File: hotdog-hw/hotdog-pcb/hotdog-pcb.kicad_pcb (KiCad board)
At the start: 2 copper layers, 202.5 x 50 mm, 29 parts, among them J1 Conn_01x01, J2 Conn_01x01, J3 Conn_01x01, J4 Conn_01x01, SW1 SW_SPST, U1 NRF24L01_Breakout, U2 ME2108A

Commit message: Simplify PCB
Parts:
- SW1: footprint Button_Switch_THT:SW_Tactile_SPST_Angled_PTS645Vx58-2LFS -> Button_Switch_THT:SW_CuK_OS102011MA1QN1_SPDT_Angled
- moved SW1 5.99 mm to (247.5, 60.0), turned to 90 degrees
- moved R6 3.54 mm to (72.5, 67.5)
- moved J1 2.50 mm to (55.0, 67.5)
- moved J2 2.50 mm to (55.0, 72.5)
- moved J3 2.50 mm to (247.5, 72.5)
- moved J4 2.50 mm to (247.5, 67.5)
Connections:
- J3 pad 1: Net-(A1-Pad4) -> Net-(A1-Pad29)
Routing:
- net Net-(A1-Pad4): track 86.2 -> 36.9 mm, vias 1 -> 0
- net Net-(A1-Pad29): track 139.6 -> 150.1 mm
- net Net-(D1-Pad2): track 94.7 -> 91.2 mm
- net Net-(BT1-Pad2): track 35.2 -> 38.4 mm
- net Net-(J1-Pad1): track 14.9 -> 12.4 mm
- net Net-(A1-Pad22): track 50.8 -> 48.8 mm
- net Net-(A1-Pad17): track 75.0 -> 73.0 mm, vias 1 -> 0
- net Net-(A1-Pad15): track 63.1 -> 64.6 mm, vias 0 -> 1
- net Net-(A1-Pad16): track 62.6 -> 64.0 mm, vias 1 -> 0
- net Net-(D1-Pad1): track 90.2 -> 89.1 mm
- net Net-(A1-Pad27): track 37.9 -> 36.8 mm
- net Net-(A1-Pad14): track 73.4 -> 74.1 mm
- net Net-(A1-Pad12): track 53.8 -> 53.1 mm, vias 1 -> 0
- net Net-(A1-Pad23): track 65.4 -> 66.0 mm, vias 1 -> 0

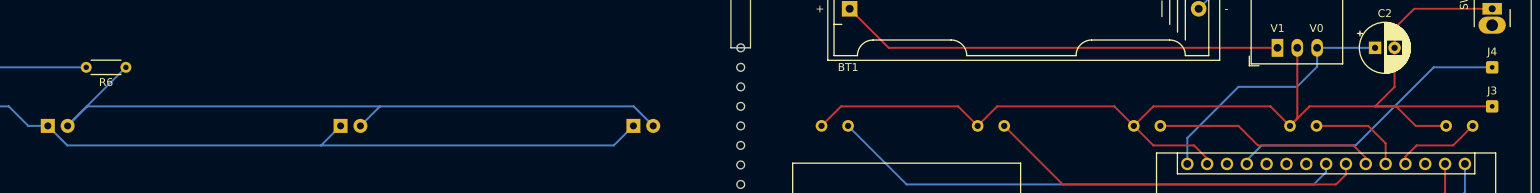
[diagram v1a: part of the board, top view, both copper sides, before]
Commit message: Smooth out a few rough spots in pcb
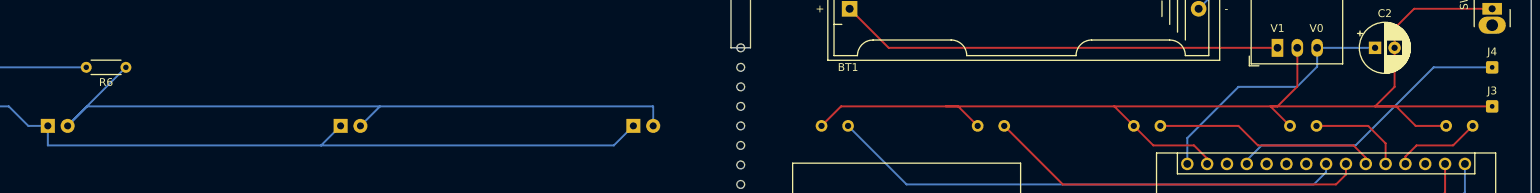
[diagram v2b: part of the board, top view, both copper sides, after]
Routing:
- net Net-(A1-Pad29): track 150.1 -> 155.1 mm
- net Net-(D1-Pad1): track 89.1 -> 90.6 mm
- net Net-(D1-Pad2): track 91.2 -> 92.6 mm
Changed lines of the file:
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@@
       (outputformat 1)
       (mirror false)
-      (drillshape 1)
+      (drillshape 0)
       (scaleselection 1)
-      (outputdirectory "")
+      (outputdirectory "out/")
     )
   )
@@
   (segment (start 230 77.5) (end 217.97 77.5) (width 0.25) (layer "B.Cu") (net 27))
   (segment (start 240 67.5) (end 230 77.5) (width 0.25) (layer "B.Cu") (net 27))
-  (segment (start 224.1 72.5) (end 247.5 72.5) (width 0.25) (layer "F.Cu") (net 29))
   (segment (start 235 70) (end 235 65) (width 0.25) (layer "F.Cu") (net 29))
   (segment (start 235.2 72.5) (end 232.5 72.5) (width 0.25) (layer "F.Cu") (net 29))
-  (segment (start 204.1 72.5) (end 201.6 75) (width 0.25) (layer "F.Cu") (net 29))
   (segment (start 232.5 72.5) (end 235 70) (width 0.25) (layer "F.Cu") (net 29))
-  (segment (start 222.54 74.06) (end 221.6 75) (width 0.25) (layer "F.Cu") (net 29))
-  (segment (start 222.54 65) (end 222.54 74.06) (width 0.25) (layer "F.Cu") (net 29))
-  (segment (start 201.6 75) (end 199.1 72.5) (width 0.25) (layer "F.Cu") (net 29))
-  (segment (start 184.1 72.5) (end 181.6 75) (width 0.25) (layer "F.Cu") (net 29))
-  (segment (start 199.1 72.5) (end 184.1 72.5) (width 0.25) (layer "F.Cu") (net 29))
+  (segment (start 222.54 65) (end 222.54 69.96) (width 0.25) (layer "F.Cu") (net 29))
   (segment (start 209.31 77.5) (end 210.99 79.18) (width 0.25) (layer "F.Cu") (net 29))
   (segment (start 221.6 75) (end 219.1 72.5) (width 0.25) (layer "F.Cu") (net 29))
   (segment (start 235 62.5) (end 237.5 60) (width 0.25) (layer "F.Cu") (net 29))
-  (segment (start 219.1 72.5) (end 204.1 72.5) (width 0.25) (layer "F.Cu") (net 29))
   (segment (start 179.1 72.5) (end 164.1 72.5) (width 0.25) (layer "F.Cu") (net 29))
   (segment (start 241.6 75) (end 237.7 75) (width 0.25) (layer "F.Cu") (net 29))
   (segment (start 201.6 75) (end 204.1 77.5) (width 0.25) (layer "F.Cu") (net 29))
+  (segment (start 201.6 75) (end 199.1 72.5) (width 0.25) (layer "F.Cu") (net 29))
   (segment (start 164.1 72.5) (end 161.6 75) (width 0.25) (layer "F.Cu") (net 29))
+  (segment (start 177.5 72.5) (end 199.1 72.5) (width 0.25) (layer "F.Cu") (net 29))
+  (segment (start 222.54 69.96) (end 220 72.5) (width 0.25) (layer "F.Cu") (net 29))
   (segment (start 237.5 60) (end 247.5 60) (width 0.25) (layer "F.Cu") (net 29))
   (segment (start 181.6 75) (end 179.1 72.5) (width 0.25) (layer "F.Cu") (net 29))
+  (segment (start 219.1 72.5) (end 247.5 72.5) (width 0.25) (layer "F.Cu") (net 29))
   (segment (start 204.1 77.5) (end 209.31 77.5) (width 0.25) (layer "F.Cu") (net 29))
-  (segment (start 224.1 72.5) (end 221.6 75) (width 0.25) (layer "F.Cu") (net 29))
+  (segment (start 220 72.5) (end 199.1 72.5) (width 0.25) (layer "F.Cu") (net 29))
   (segment (start 237.7 75) (end 235.2 72.5) (width 0.25) (layer "F.Cu") (net 29))
   (segment (start 210.99 79.18) (end 210.99 79.87) (width 0.25) (layer "F.Cu") (net 29))
@@
   (segment (start 208.45 79.87) (end 208.45 76.55) (width 0.25) (layer "B.Cu") (net 30))
   (segment (start 60 75) (end 62.5 75) (width 0.25) (layer "B.Cu") (net 31))
+  (segment (start 62.5 77.5) (end 97.5 77.5) (width 0.25) (layer "B.Cu") (net 31))
   (segment (start 97.5 77.5) (end 100 75) (width 0.25) (layer "B.Cu") (net 31))
   (segment (start 97.5 77.5) (end 135 77.5) (width 0.25) (layer "B.Cu") (net 31))
   (segment (start 57.5 72.5) (end 60 75) (width 0.25) (layer "B.Cu") (net 31))
   (segment (start 55 72.5) (end 57.5 72.5) (width 0.25) (layer "B.Cu") (net 31))
-  (segment (start 65 77.5) (end 97.5 77.5) (width 0.25) (layer "B.Cu") (net 31))
   (segment (start 135 77.5) (end 137.5 75) (width 0.25) (layer "B.Cu") (net 31))
-  (segment (start 62.5 75) (end 65 77.5) (width 0.25) (layer "B.Cu") (net 31))
+  (segment (start 62.5 75) (end 62.5 77.5) (width 0.25) (layer "B.Cu") (net 31))
   (segment (start 65.04 75) (end 67.5 72.54) (width 0.25) (layer "B.Cu") (net 32))
   (segment (start 67.5 72.54) (end 67.5 72.5) (width 0.25) (layer "B.Cu") (net 32))
   (segment (start 72.5 67.5) (end 65.04 74.96) (width 0.25) (layer "B.Cu") (net 32))
   (segment (start 102.54 75) (end 105 72.54) (width 0.25) (layer "B.Cu") (net 32))
-  (segment (start 105 72.5) (end 137.54 72.5) (width 0.25) (layer "B.Cu") (net 32))
   (segment (start 67.5 72.5) (end 105 72.5) (width 0.25) (layer "B.Cu") (net 32))
+  (segment (start 140 72.5) (end 140.04 72.54) (width 0.25) (layer "B.Cu") (net 32))
+  (segment (start 140.04 72.54) (end 140.04 75) (width 0.25) (layer "B.Cu") (net 32))
+  (segment (start 105 72.5) (end 140 72.5) (width 0.25) (layer "B.Cu") (net 32))
   (segment (start 105 72.54) (end 105 72.5) (width 0.25) (layer "B.Cu") (net 32))
-  (segment (start 137.54 72.5) (end 140.04 75) (width 0.25) (layer "B.Cu") (net 32))
   (segment (start 65.04 74.96) (end 65.04 75) (width 0.25) (layer "B.Cu") (net 32))
   (segment (start 55 67.5) (end 67.42 67.5) (width 0.25) (layer "B.Cu") (net 33))
